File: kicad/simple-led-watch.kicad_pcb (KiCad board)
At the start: 4 copper layers, 32.8 x 32.6 mm, 179 parts, among them P1 BATTERY, P2 SWD, P3 USB_OTG, Q1 MMBT3904, Q2 MMBT3904, SW1 SPST-4PIN, SW2 SPST-4PIN, SW3 SPST-4PIN, SW4 SPST-4PIN, U1 MCP73832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

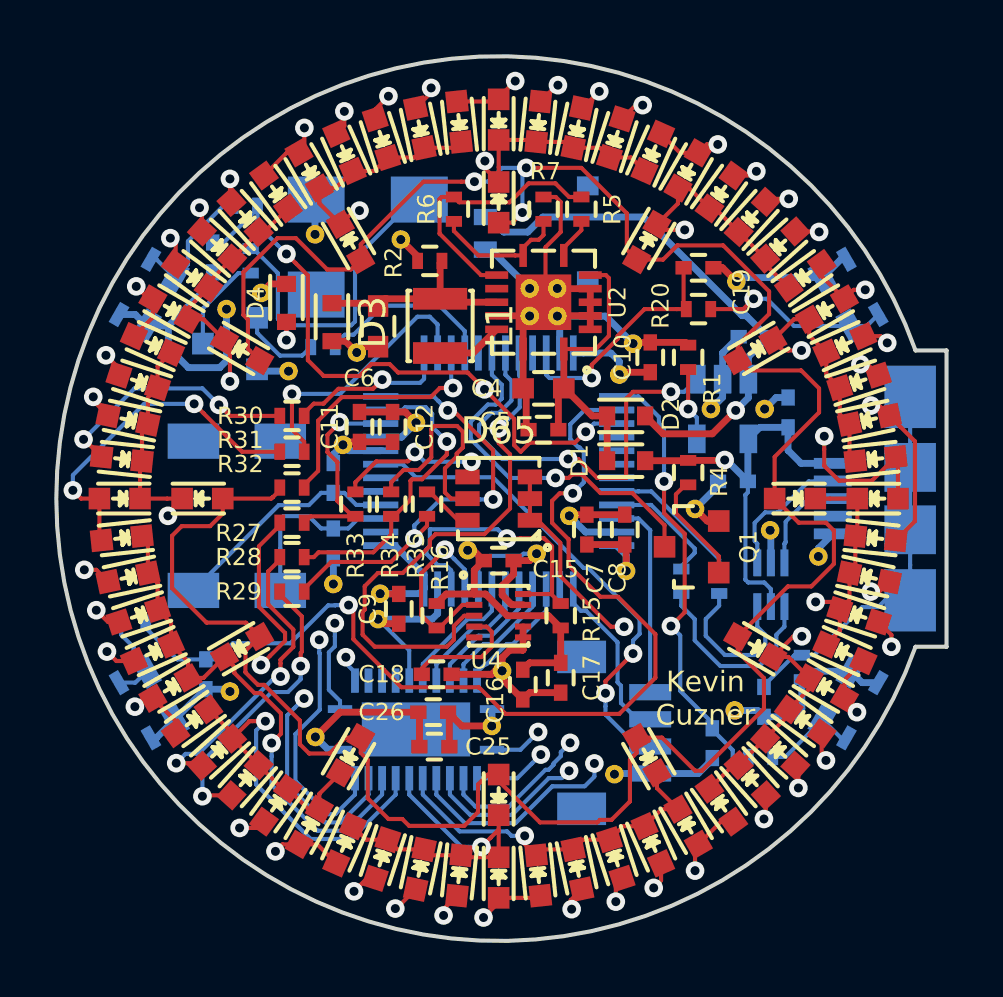
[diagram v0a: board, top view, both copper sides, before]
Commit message: Changed out D65 RGB LED for a shorter 0606 part
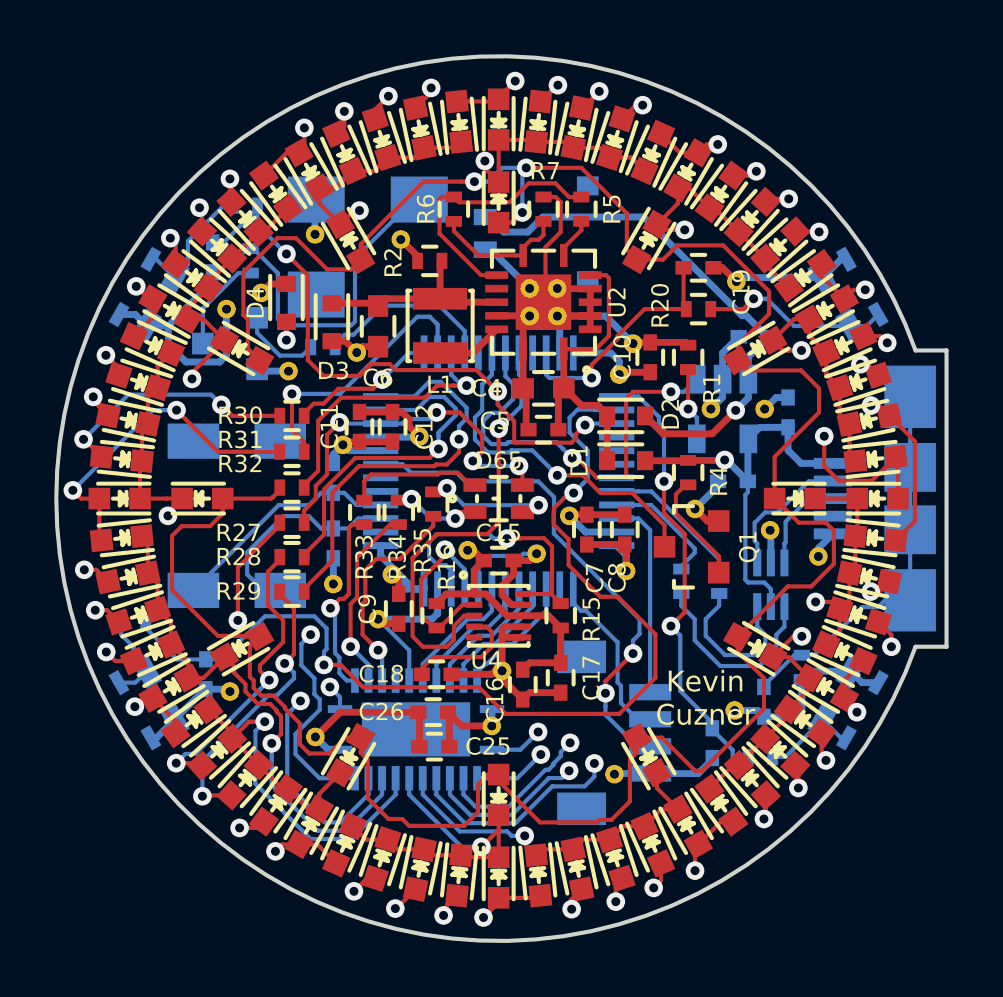
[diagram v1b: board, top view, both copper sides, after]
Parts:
- D65: value LED_RGB -> QBLP600-RGB; footprint simple-led-watch:PLCC6 -> simple-led-watch:LED-0606
- moved REF** 0.83 mm to (161.2, 91.7)
- moved REF** 0.52 mm to (162.2, 86.6)
- moved R33 0.45 mm to (160.1, 89.4)
- moved R34 0.41 mm to (161.4, 89.4)
- moved R35 0.23 mm to (162.7, 89.1)
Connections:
- D65 pad 1: /LEDs/LED_RGB_C -> /Control/LED_A0
- D65 pad 2: /LEDs/LED_RGB_C -> /LEDs/LED_R_R
- D65 pad 3: /LEDs/LED_RGB_C -> /LEDs/LED_G_R
- D65 pad 4: /LEDs/LED_R_A -> /LEDs/LED_B_R
- R33 pad 1: /LEDs/LED_R_A -> /LEDs/LED_R_R
- R33 pad 2: /Control/LED_A0 -> /LEDs/LED_R_C
- R34 pad 1: /LEDs/LED_G_A -> /LEDs/LED_G_R
- R34 pad 2: /Control/LED_A1 -> /LEDs/LED_G_C
- R35 pad 1: /LEDs/LED_B_A -> /LEDs/LED_B_R
- R35 pad 2: /Control/LED_A2 -> /LEDs/LED_B_C
- U6 pad 14: /LEDs/LED_RGB_C -> /LEDs/LED_R_C
- U6 pad 15: Net-(U6-Pad15) -> /LEDs/LED_G_C
- U6 pad 16: Net-(U6-Pad16) -> /LEDs/LED_B_C
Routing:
- net /LEDs/LED_RGB_C: track 28.5 -> 0.00 mm, vias 2 -> 0
- net /LEDs/LED_G_A: track 8.33 -> 0.00 mm
- net /LEDs/LED_B_C: track 0.00 -> 7.95 mm, vias 0 -> 1
- net /LEDs/LED_R_C: track 0.00 -> 7.48 mm, vias 0 -> 1
- net /LEDs/LED_SEG11: track 36.8 -> 44.2 mm
- net /LEDs/LED_G_C: track 0.00 -> 7.00 mm, vias 0 -> 1
- net /Control/LED_A0: track 7.77 -> 13.8 mm, vias 1 -> 4
- net /LEDs/LED_R_A: track 5.92 -> 0.00 mm, vias 2 -> 0
- net /LEDs/LED_R_R: track 0.00 -> 5.09 mm
- net /LEDs/LED_B_R: track 0.00 -> 5.04 mm, vias 0 -> 2
- net /LEDs/LED_SEG9: track 28.1 -> 32.1 mm
- net /Control/~ACCEL_INT: track 19.8 -> 16.4 mm
- net /LEDs/LED_G_R: track 0.00 -> 3.28 mm, vias 0 -> 2
- net /LEDs/LED_A_R0: track 108.5 -> 106.2 mm
- net /LEDs/LED_B_A: track 1.93 -> 0.00 mm
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
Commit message: Upgrade to latest kicad, add some measurements
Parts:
- added REF**: 1PIN_VIA, simple-led-watch:1PIN_VIA, F.Cu at (172.1, 94.7)
- C20: moved to F.Cu
- moved C20 2.17 mm to (172.7, 95.8), turned to 90 degrees
- moved P2 1.14 mm to (168.4, 97.5)
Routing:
- net /Control/BTN2: track 37.4 -> 34.0 mm
- net /Control/SWCLK: track 6.37 -> 8.14 mm, vias 0 -> 2
- net /LEDs/LED_SEG1: track 41.5 -> 40.1 mm
- net /LEDs/LED_SEG0: track 49.0 -> 47.5 mm
- net GND: track 101.1 -> 100.0 mm

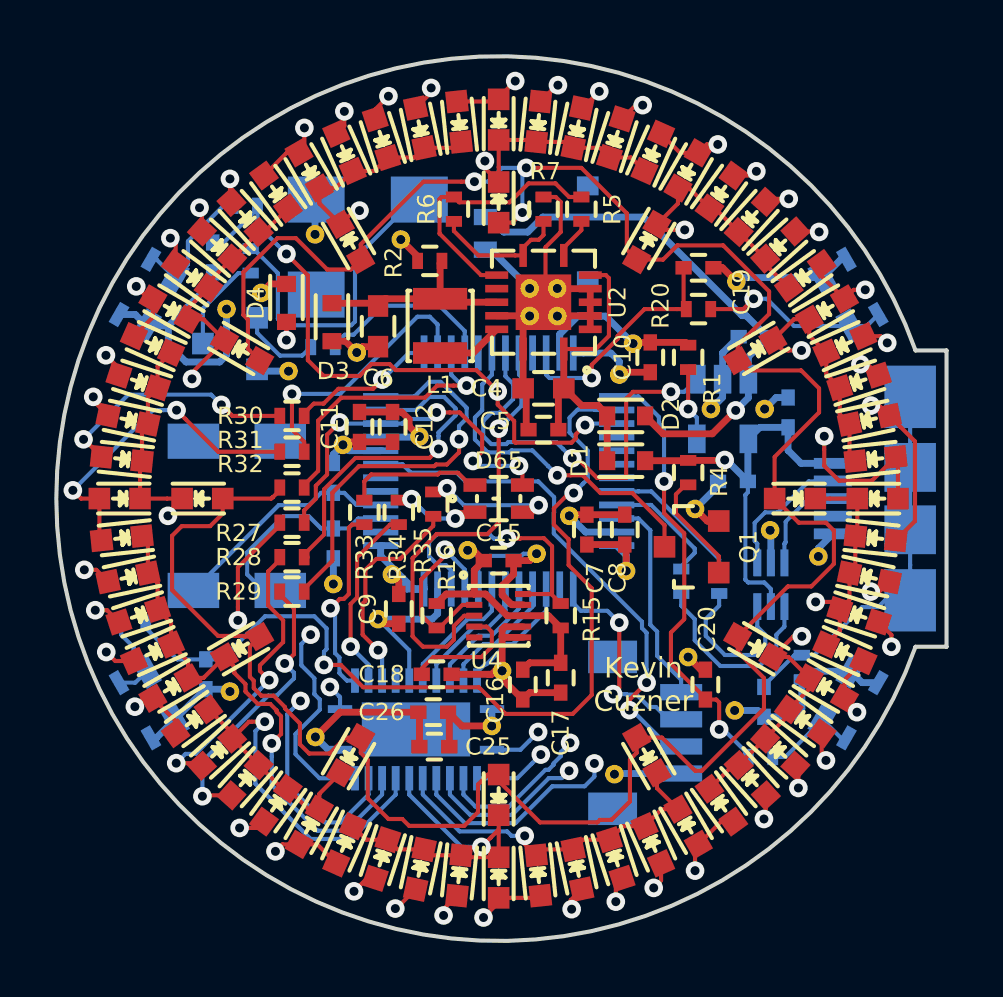
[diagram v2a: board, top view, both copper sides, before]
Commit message: Checked layout and reference designs, swapped crystal and RGB LED
ST has a list of suggested crystals which are known to work with the
STM32L0 family. I selected one of those and it is significantly
smaller in all dimensions.

The RGB LED had too high of a green voltage. I swapped it out for a
slightly more expensive one with the same footprint that had startlingly
low green and blue forward voltages.

For layout changes:
- Fixed regulator footprint silkscreen
- Fixed regulator layout to be closer to reference design
- Fixed inductor silkscreen
- Moved accelerometer downward to accomodate capacitors above
- Fixed accelerometer layout to have no traces beneath
- Fixed accelerometer silkscreen
- Fixed LED silkscreen
- General small silkscreen edits, such as shifting text around

I've also chosen parts and values for all resistors and capacitors.
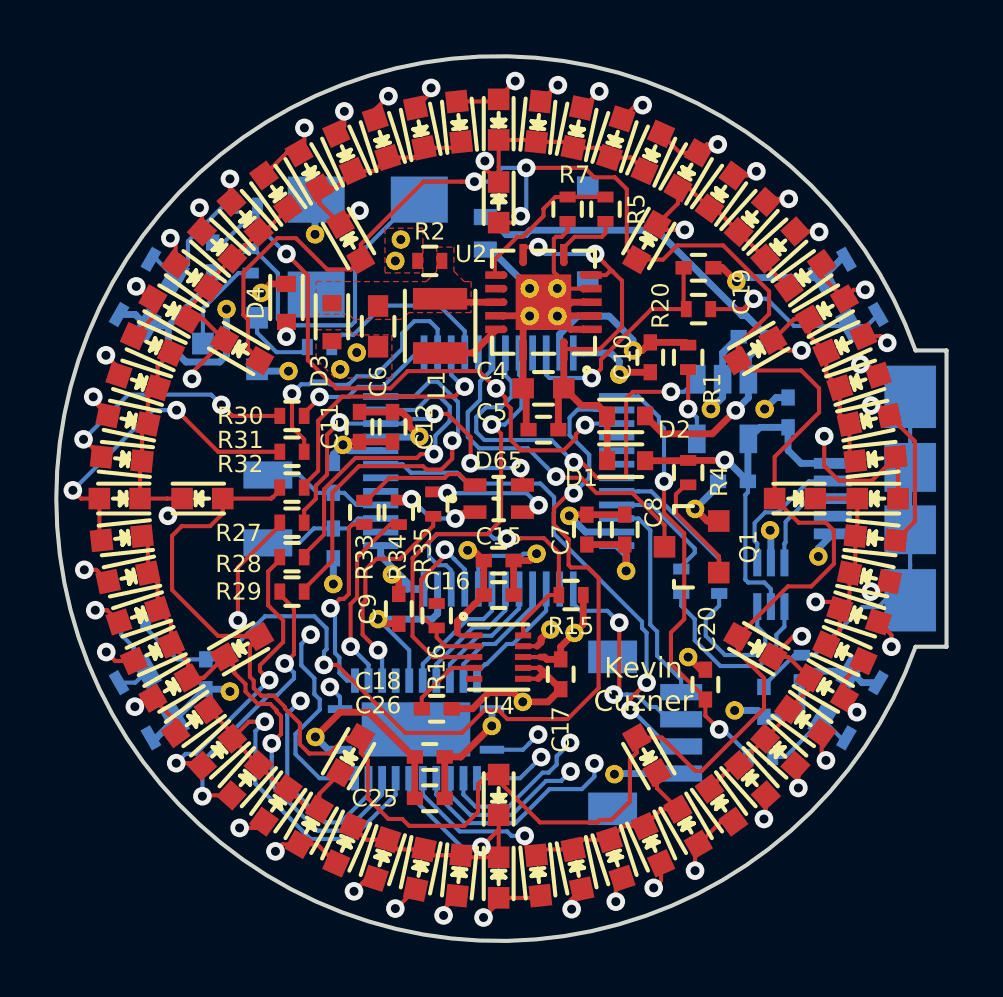
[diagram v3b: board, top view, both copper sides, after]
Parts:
- removed R6: 0, Resistors_SMD:R_0402
- added REF**: 1PIN_VIA, simple-led-watch:1PIN_VIA, F.Cu at (167.0, 93.7)
- added REF**: 1PIN_VIA, simple-led-watch:1PIN_VIA, F.Cu at (167.9, 93.9)
- added REF**: 1PIN_VIA, simple-led-watch:1PIN_VIA, F.Cu at (159.3, 84.1)
- added REF**: 1PIN_VIA, simple-led-watch:1PIN_VIA, F.Cu at (161.3, 80.1)
- C1: value 1u -> 4.7u
- C13, C14: value C -> 8.2p
- D65: value QBLP600-RGB -> APTF1616LSEEZGKQBKC
- R13: value R -> 0
- R27, R28, R29, R30, R31, R33: value R -> 150
- R32: value R -> 47
- R34, R35: value R -> 68
- R5: value 6.3M -> 825K
- R7: value 3.67M -> 475K
- U3: value STM32L052CxTx -> STM32L052x8
- Y1: footprint simple-led-watch:XTAL-CPFB -> simple-led-watch:Crystal-Abracon-ABS07
- moved C16 3.42 mm to (165.1, 92.5), turned to 0 degrees
- moved C25 1.91 mm to (162.6, 99.9)
- moved C26 1.66 mm to (162.6, 98.4)
- moved U4 1.52 mm to (165.1, 94.7)
- moved REF** 1.37 mm to (166.0, 96.4)
- moved C18 1.27 mm to (162.8, 96.6)
- moved Y1 1.17 mm to (156.6, 89.3)
- moved R5 0.89 mm to (169.0, 78.2)
- moved R7 0.89 mm to (167.6, 78.2), turned to 270 degrees
- moved R15 0.85 mm to (167.8, 92.5), turned to 180 degrees
- moved REF** 0.25 mm to (170.1, 83.4)
- moved C17 0.13 mm to (167.4, 95.4)
- moved R18 0.13 mm to (158.5, 83.3)
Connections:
- R7 pad 1: /Power Supply/+3.3V_REG_VOK_SET -> /Power Supply/+3.3V_REG_VOUT_SET
- U2 pad 8: /Power Supply/+3.3V_REG_VOK_SET -> /Power Supply/+3.3V_REG_SRC
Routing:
- net /Power Supply/+3.3V_REG_OUT: track 7.70 -> 2.32 mm
- net /Power Supply/+3.3V_REG_VOK_SET: track 5.01 -> 0.00 mm
- net /Power Supply/+3.3V_REG_SRC: track 11.5 -> 15.9 mm, vias 0 -> 2
- net /Power Supply/+3.3V_REG_VOUT_SET: track 9.85 -> 5.77 mm
- net /Control/STM32_OSC32-: track 8.58 -> 4.62 mm
- net /Control/STM32_OSC32+: track 8.09 -> 4.53 mm
- net +3V3: track 33.6 -> 31.8 mm
- net Net-(C18-Pad1): track 4.40 -> 2.80 mm
- net /Control/BTN2: track 34.0 -> 35.5 mm
- net GND: track 100.0 -> 98.8 mm
- net /Power Supply/+3.3V_REG_VRDIV: track 1.52 -> 2.41 mm
- net /Control/I2C_SDA: track 10.4 -> 11.2 mm
- net /LEDs/LED_A_R5: track 96.8 -> 97.4 mm
- net /Control/LED_A0: track 13.8 -> 13.2 mm
- added copper zone on F.Cu, net +3V3
- added copper zone on F.Cu, net /Power Supply/+3.3V_REG_OUT
- added copper zone on F.Cu, net GND
